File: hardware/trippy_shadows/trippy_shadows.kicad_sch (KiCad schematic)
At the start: 32 parts, among them J1 ISP, J10 JST conn, J2 GPIO, J3 DEBUG, J4 PWR, J5 JST conn, J6 JST conn, J7 JST conn, J8 JST conn, J9 JST conn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

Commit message: Commit latest board design
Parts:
- removed J2: GPIO, Connector_PinHeader_2.54mm:PinHeader_2x04_P2.54mm_Vertical, symbol Connector_Generic:Conn_02x04_Odd_Even
- removed J3: DEBUG, Connector_PinHeader_2.54mm:PinHeader_2x03_P2.54mm_Vertical, symbol Connector_Generic:Conn_02x03_Odd_Even
- added J3: Debug, Connector_PinHeader_2.54mm:PinHeader_1x03_P2.54mm_Vertical, symbol Connector_Generic:Conn_01x03
- added R10, R11, R12, R13, R8, R9: 10k, Resistor_SMD:R_0805_2012Metric, symbol Device:R
- added RV1: 10k, Potentiometer_THT:Potentiometer_Alps_RK09K_Single_Vertical, symbol Device:R_Potentiometer
- J10, J5, J6, J7, J8, J9: value JST conn -> S2B-PH-KL(LF)(SN); footprint Connector_JST:JST_PH_B2B-PH-K_1x02_P2.00mm_Vertical -> Connector_JST:JST_PH_S2B-PH-K_1x02_P2.00mm_Horizontal; now fitted
- J4: value PWR -> JST_PH_B2B-PH-K; footprint TerminalBlock:TerminalBlock_bornier-2_P5.08mm -> Connector_JST:JST_PH_B2B-PH-K_1x02_P2.00mm_Vertical; now fitted
- R2, R3, R4, R5, R6, R7: value R -> 2.7k; now fitted
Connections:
- net DRV0: now also U1.2 (PD4), R8.2; no longer U1.23 (PC0)
- net DRV1: now also U1.1 (PD3), R9.2; no longer U1.24 (PC1)
- net DRV2: now also U1.26 (PC3), R10.2; no longer U1.25 (PC2)
- net DRV3: now also U1.23 (PC0), R13.2; no longer U1.26 (PC3)
- net DRV4: now also U1.24 (PC1), R12.2; no longer U1.1 (PD3)
- net DRV5: now also U1.25 (PC2), R11.2; no longer U1.2 (PD4)
- net GND: now also J3.1 (Pin_1), R10.1, R11.1, R12.1, R13.1, R8.1, R9.1, RV1.3
- net RXD: now also J3.2 (Pin_2)
- net TXD: now also J3.3 (Pin_3)
- net VCC: now also U1.20 (AREF), RV1.1
- net at U1.22 (ADC7): now also RV1.2
- net GPIO0: no longer names the net of U1.12 (PB0)
- net GPIO1: no longer names the net of U1.13 (PB1)
- net GPIO2: no longer names the net of U1.14 (PB2)
- net GPIO3: no longer names the net of U1.7 (XTAL1/PB6)
- net GPIO4: no longer names the net of U1.8 (XTAL2/PB7)
- net GPIO5: no longer names the net of U1.10 (PD6)
- net GPIO6: no longer names the net of U1.11 (PD7)
- net INT0: no longer names the net of U1.32 (PD2)
- net SCL: no longer names the net of U1.28 (PC5)
- net SDA: no longer names the net of U1.27 (PC4)
- no-connect marks 10 -> 18
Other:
- moved on the sheet: C1, C2, C3, C4, C7, C8, R1, U1, U2, U3, U5, U6

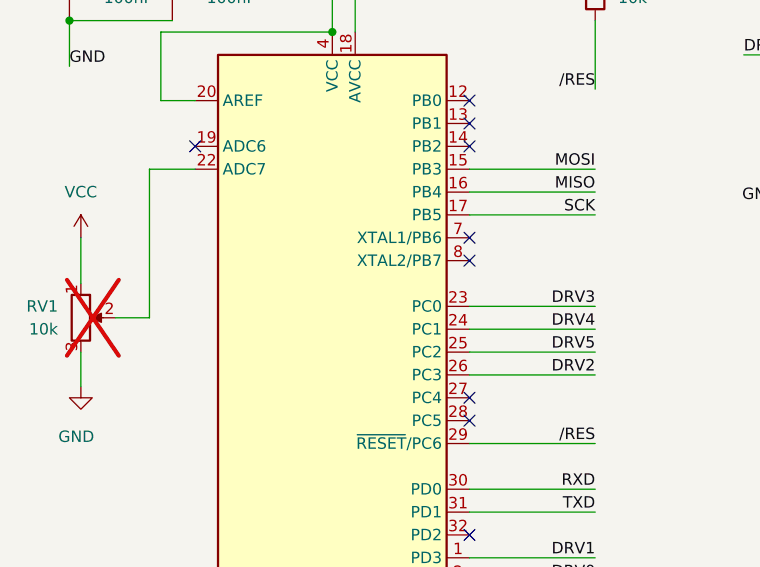
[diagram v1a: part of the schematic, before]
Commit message: Updated schematic to move to working adc
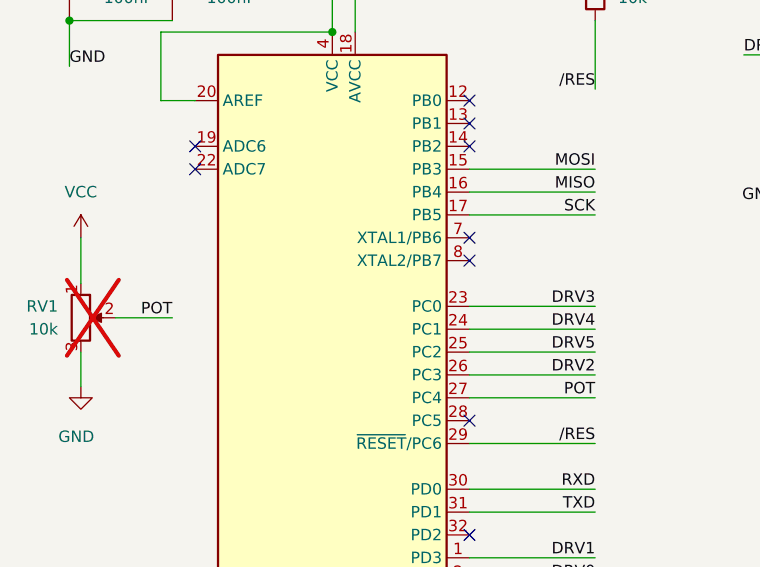
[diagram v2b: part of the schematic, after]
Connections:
- net at U1.22 (ADC7): no longer RV1.2
- net POT: now reaches U1.27 (PC4)
- net POT: now also RV1.2
